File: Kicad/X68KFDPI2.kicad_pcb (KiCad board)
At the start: 2 copper layers, 86.3 x 106.4 mm, 31 parts, among them J1 HxC Connector, J11 Micro_SD_Card, J13 FD Int/Ext (0,1/2,3), J2 FD Ext Connector, J3 FD00, J4 FD01, J7 LedFD0, J8 LedFD1, J9 FloppyPWR, SW1 SW_Push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

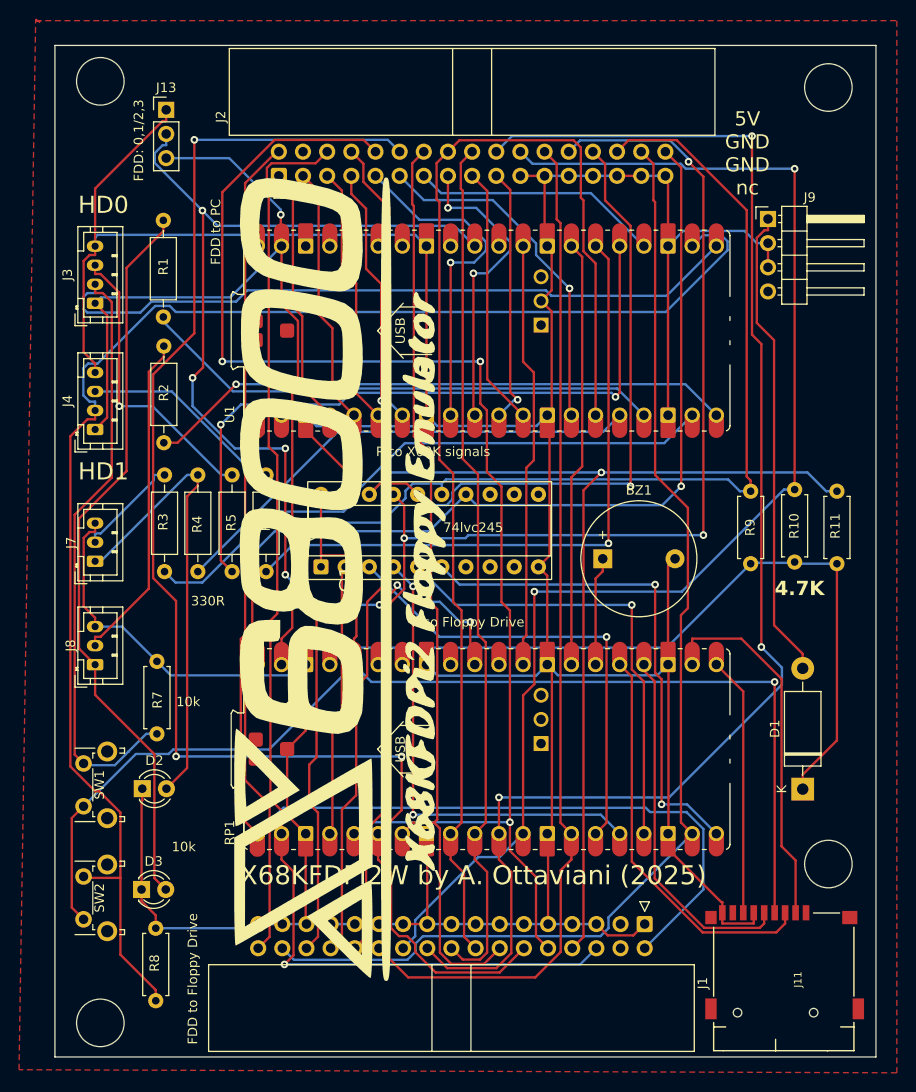
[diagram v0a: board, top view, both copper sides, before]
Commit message: Added 74lvc245 dir control
Test in progress for avoiding conflict when 2 x68kfdpi2w are used togheter
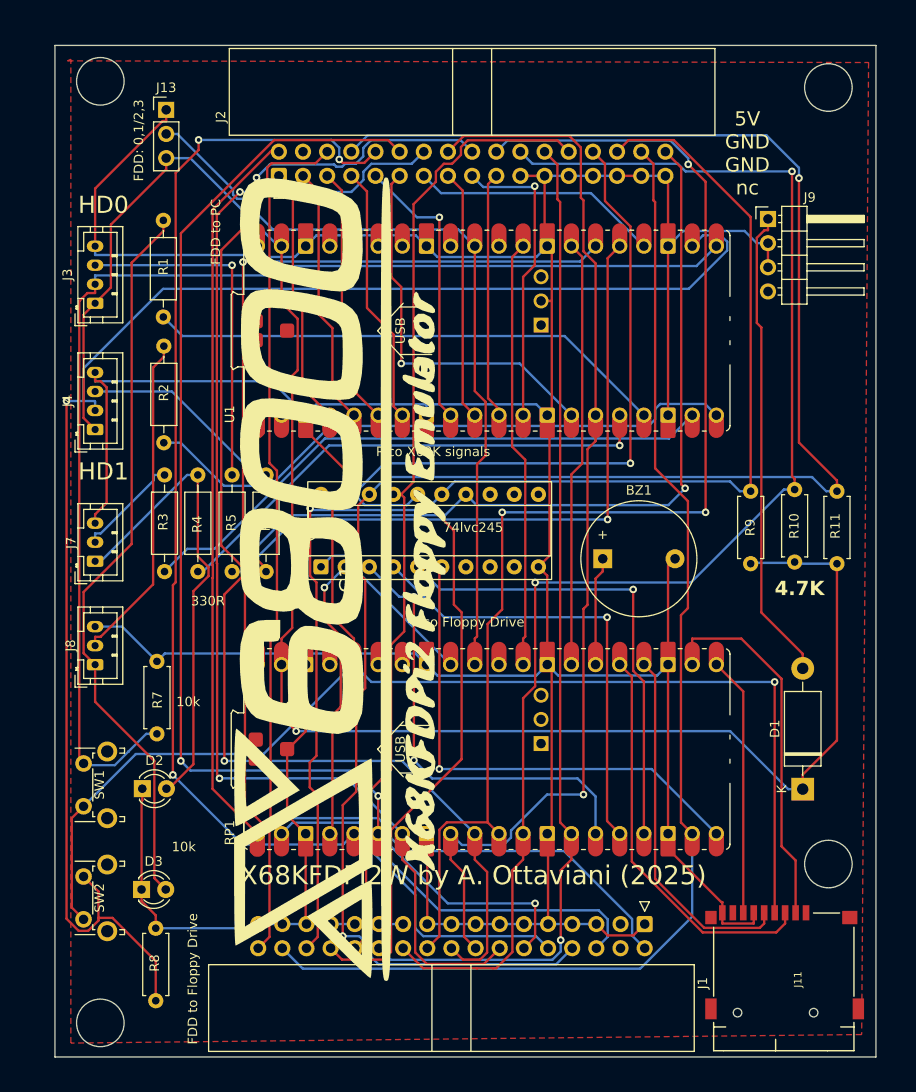
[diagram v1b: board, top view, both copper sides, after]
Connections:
- RP1 pad 32: unconnected-(RP1-G27-Pad32)_1 -> LVC245_EN
- U2 pad 1: +3.3V -> LVC245_EN
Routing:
- net ~{INDEX}: track 140.8 -> 210.2 mm, vias 1 -> 2
- net ~{DIR}: track 91.4 -> 137.2 mm, vias 0 -> 2
- net ~{TRK0}: track 136.0 -> 102.6 mm, vias 3 -> 0
- net Int/Ext: track 115.0 -> 84.2 mm, vias 7 -> 0
- net ~{DS2}: track 99.1 -> 129.1 mm, vias 0 -> 2
- net GND: track 487.0 -> 509.0 mm
- net LVC245_EN: track 0.00 -> 20.9 mm
- net ~{MOTOR}: track 132.1 -> 114.6 mm, vias 0 -> 1
- net ~{WPROT}: track 116.1 -> 132.4 mm
- net ~{DS1}: track 150.5 -> 135.6 mm
- net ~{STEP}: track 148.5 -> 135.7 mm
- net ~{DENSITY}: track 139.9 -> 127.2 mm
- net BT_FD0: track 138.0 -> 130.0 mm
- net ~{DS0}: track 147.0 -> 140.3 mm
- net BT_FD1: track 157.2 -> 163.3 mm, vias 0 -> 1
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
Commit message: Fix for drive 0/1-2/3
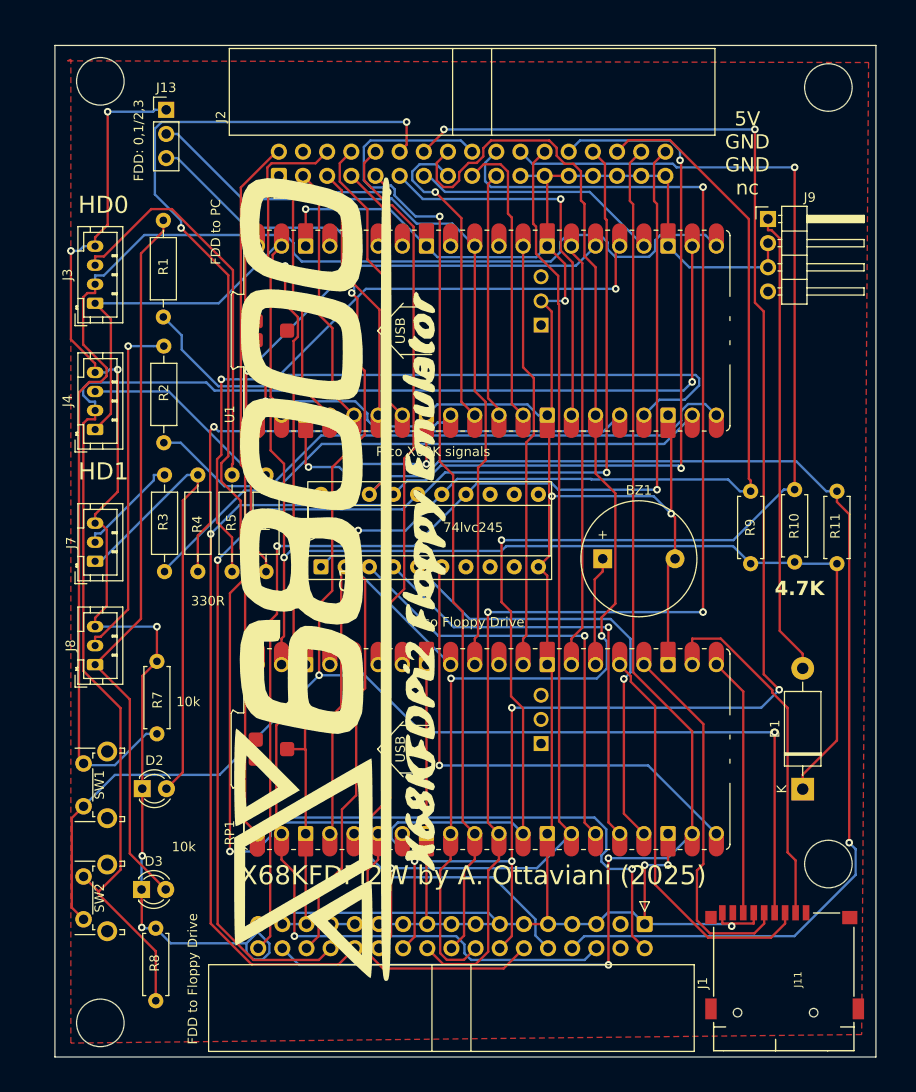
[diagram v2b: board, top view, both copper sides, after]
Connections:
- J13 pad 3: 5vtoPico -> +3.3V
- U1 pad 36: unconnected-(U1-3V3-Pad36)_1 -> +3.3V
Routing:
- net ~{TRK0}: track 102.6 -> 157.2 mm, vias 0 -> 3
- net +3.3V: track 136.1 -> 189.4 mm, vias 1 -> 4
- net ~{INDEX}: track 210.2 -> 165.6 mm, vias 2 -> 1
- net ~{DS2}: track 129.1 -> 164.9 mm, vias 2 -> 5
- net ~{DS0}: track 140.3 -> 105.6 mm, vias 3 -> 0
- net ~{DIR}: track 137.2 -> 105.3 mm, vias 2 -> 1
- net ~{EJECT}: track 31.4 -> 63.0 mm, vias 1 -> 3
- net 5vtoPico: track 193.5 -> 168.4 mm
- net ~{DS1}: track 135.6 -> 160.0 mm
- net ~{MOTOR}: track 114.6 -> 129.1 mm, vias 1 -> 2
- net LEDFD1: track 56.4 -> 70.3 mm
- net ~{WDATA}: track 147.2 -> 158.5 mm, vias 2 -> 3
- net BT_FD0: track 130.0 -> 140.3 mm
- net BT_FD1: track 163.3 -> 154.5 mm
- net LEDFD0: track 53.0 -> 61.1 mm
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
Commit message: fix+moved button connectors
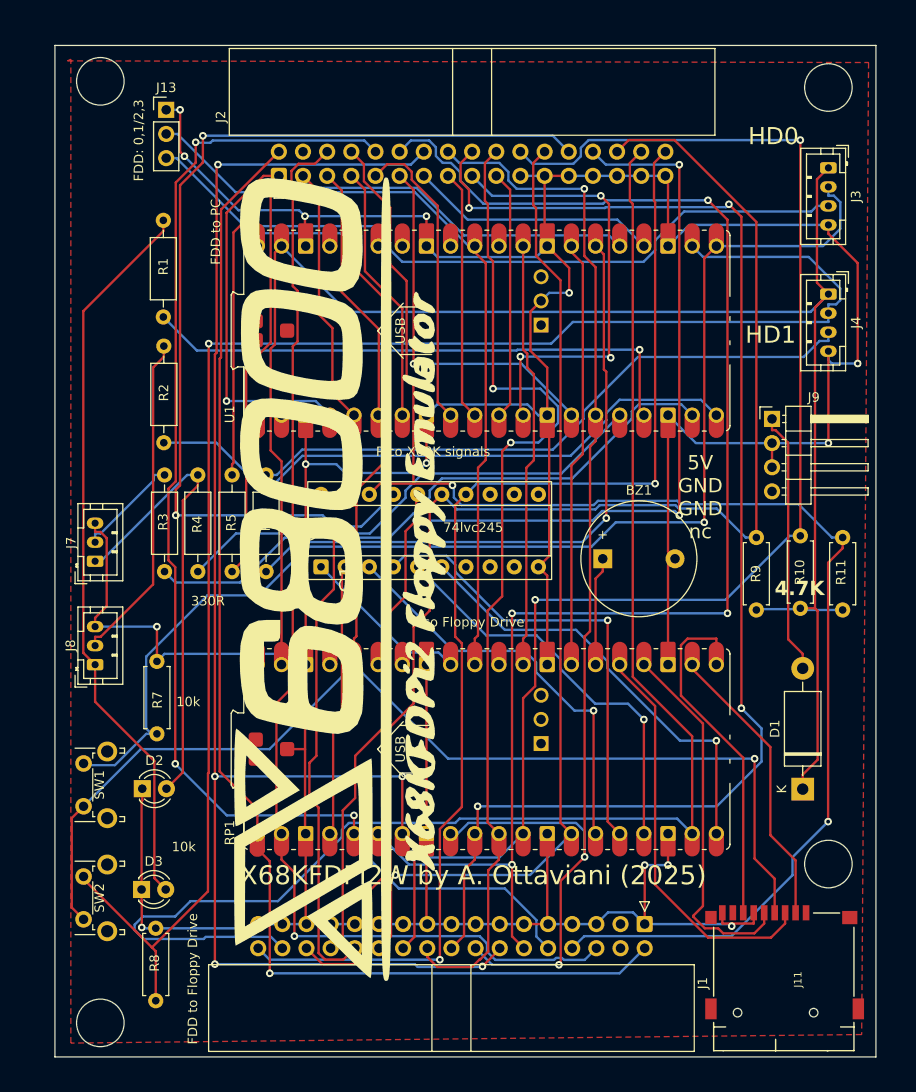
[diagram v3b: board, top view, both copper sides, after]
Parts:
- moved J3 78.4 mm to (150.0, 52.9), turned to -90 degrees
- moved J4 78.4 mm to (150.0, 66.2), turned to -90 degrees
- moved J9 21.0 mm to (144.1, 79.3)
- moved R10 4.90 mm to (147.1, 99.2)
- moved R9 4.90 mm to (142.4, 99.4)
- moved R11 4.90 mm to (151.5, 99.4)
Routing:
- net Net-(J3-Pin_3): track 41.7 -> 94.1 mm, vias 0 -> 1
- net Net-(J4-Pin_3): track 21.6 -> 66.3 mm
- net ~{DIR}: track 105.3 -> 142.2 mm, vias 1 -> 4
- net ~{STEP}: track 138.4 -> 104.8 mm, vias 3 -> 2
- net ~{DS0}: track 105.6 -> 137.9 mm, vias 0 -> 3
- net ~{EJECT}: track 63.0 -> 33.5 mm, vias 3 -> 0
- net ~{SIDE}: track 132.6 -> 157.9 mm, vias 2 -> 0
- net GND: track 516.3 -> 492.2 mm, vias 15 -> 14
- net +5V: track 49.0 -> 27.8 mm
- net 5vtoPico: track 168.4 -> 186.1 mm, vias 1 -> 0
- net BT_FD1: track 154.5 -> 171.8 mm
- net ~{ERROR}: track 32.5 -> 49.3 mm, vias 0 -> 3
- net BT__LED_FD0: track 72.7 -> 84.2 mm, vias 2 -> 1
- net ~{OPT0}: track 29.0 -> 40.0 mm, vias 0 -> 1
- net ~{INDEX}: track 165.6 -> 155.3 mm, vias 1 -> 2
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
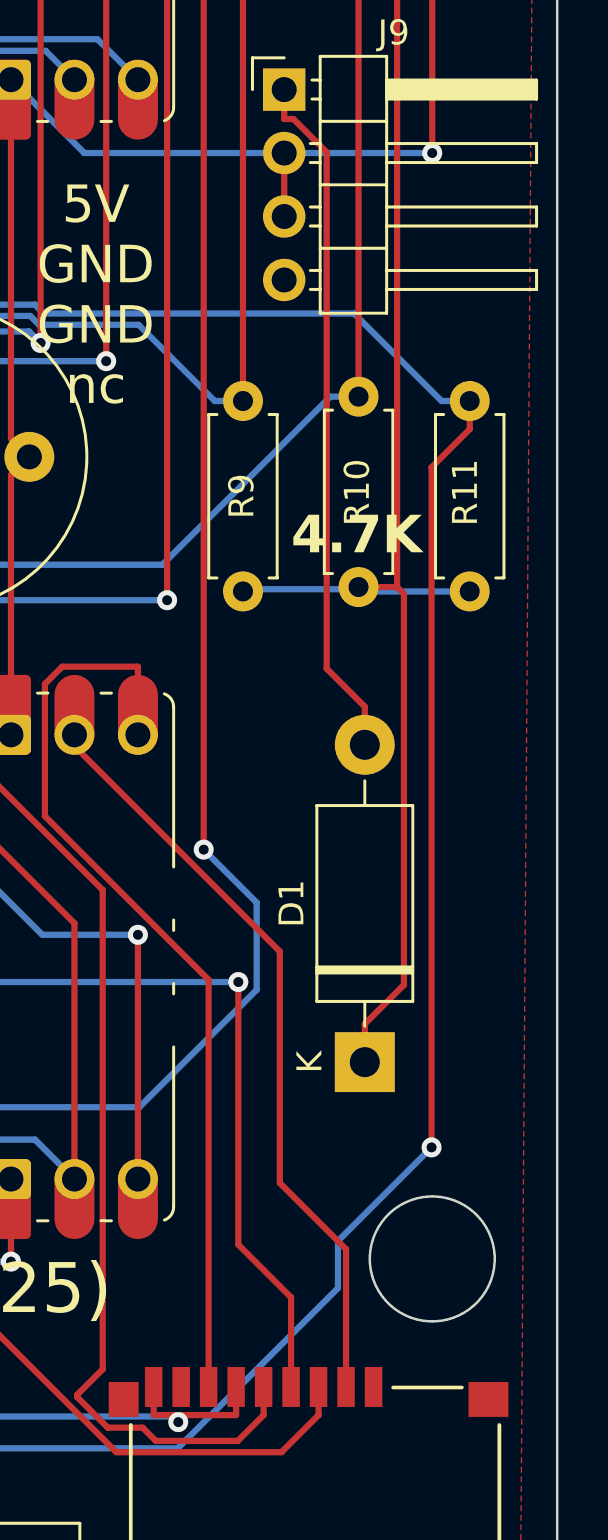
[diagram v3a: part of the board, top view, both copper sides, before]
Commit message: Fixed fdd power connector
Fixed 5vsb to gnd in fdd power connector for some models
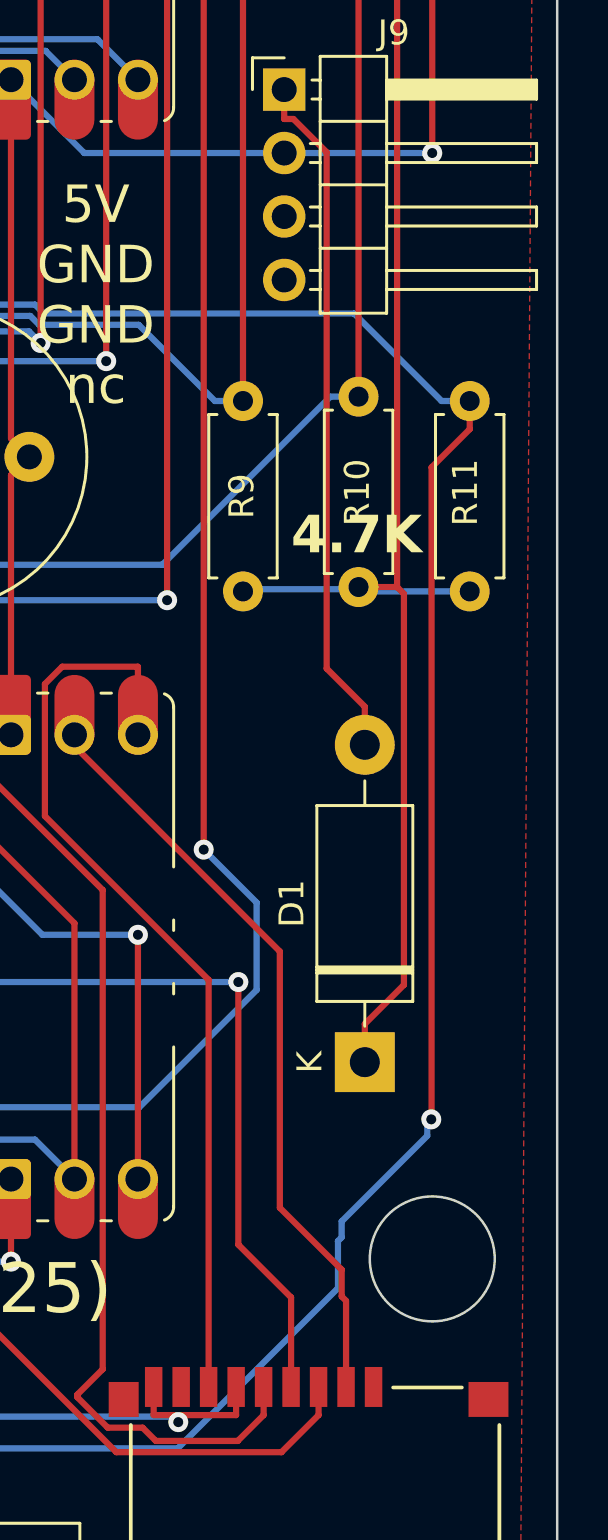
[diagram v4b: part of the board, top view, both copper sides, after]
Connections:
- J9 pad 3: GND -> unconnected-(J9-Pin_3-Pad3)
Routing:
- net GND: track 492.2 -> 489.6 mm
